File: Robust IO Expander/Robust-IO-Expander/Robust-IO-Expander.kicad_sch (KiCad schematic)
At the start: 69 parts, among them J1 Input Headers, J10 Right SPI In, J11 SPI Terminal, J12 Power Input, J2 CS Inputs, J3 CS Terminal, J4 SPI Inputs, J5 Input Terminal, J6 Output Terminal, J7 Ouput Headers, J8 Power Input, J9 Left SPI Out, U1 MCP23S17_SS, U10 LTV-847S, U11 R-78B3.3-2.0, U12 NUP4202, U13 NUP4202, U14 BZX84C5V1TS-7-F, U15 BZX84C5V1TS-7-F, U2 MCP23S17_SS, U3 LTV-847S, U4 LTV-847S, U5 LTV-847S, U6 LTV-847S, U7 LTV-847S, U8 LTV-847S, U9 LTV-847S

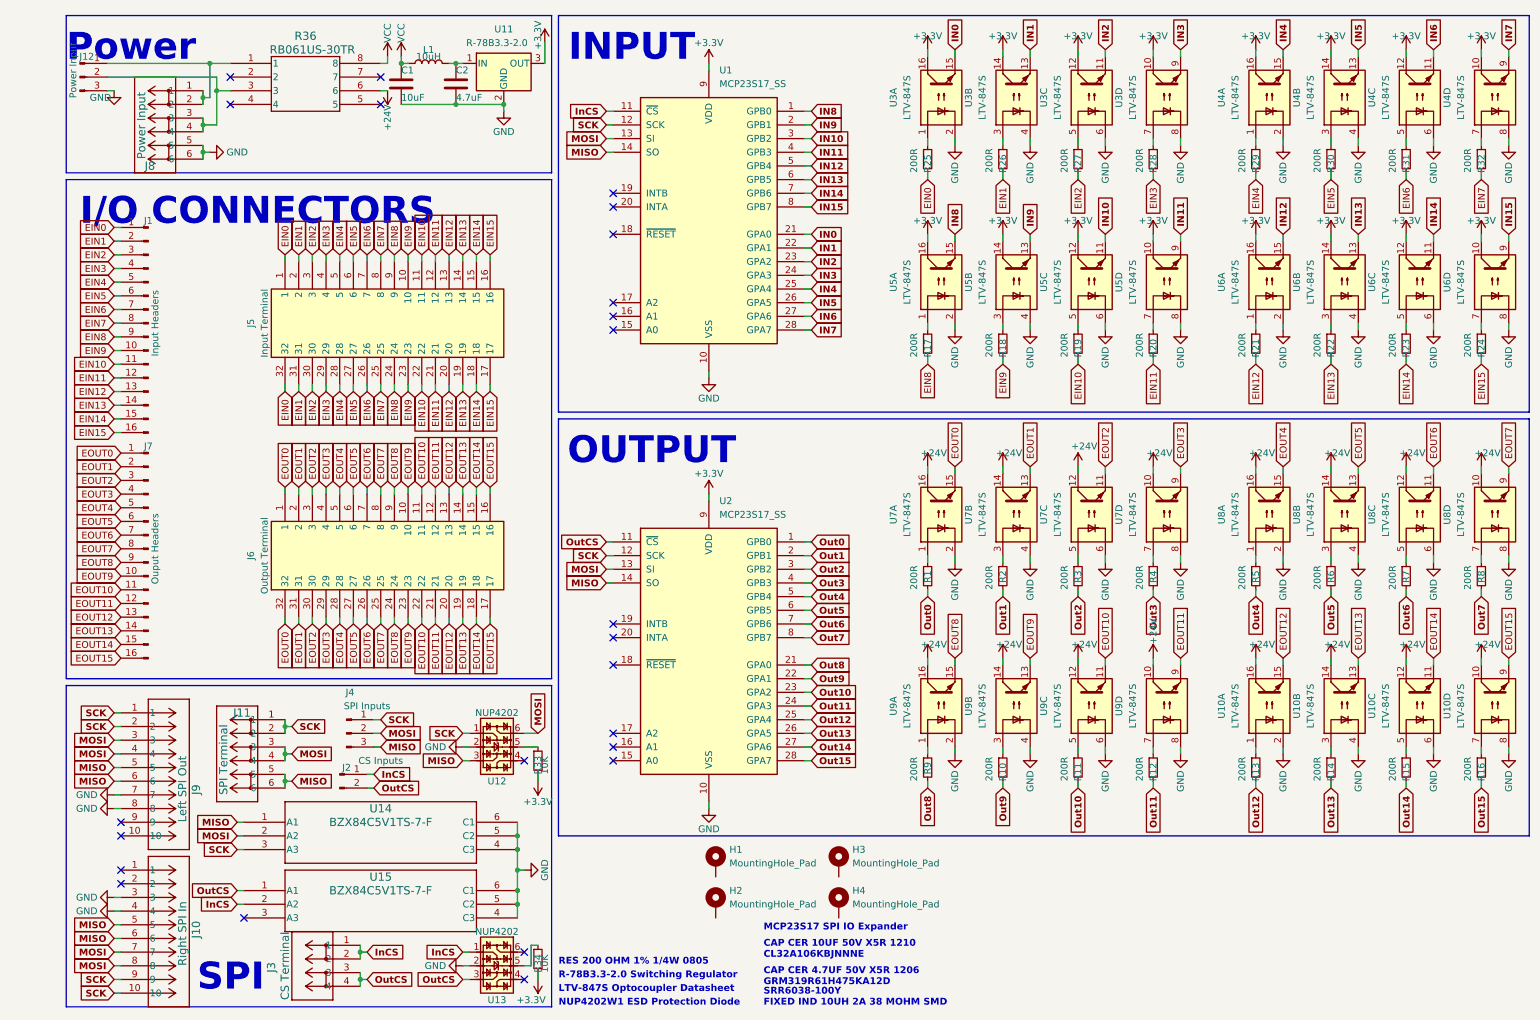
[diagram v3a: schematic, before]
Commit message: Updates
AD 12/11/23
1K Resistors inserted for 200R
0603 components Error correct to 0805
Post DFM Analysis Changes
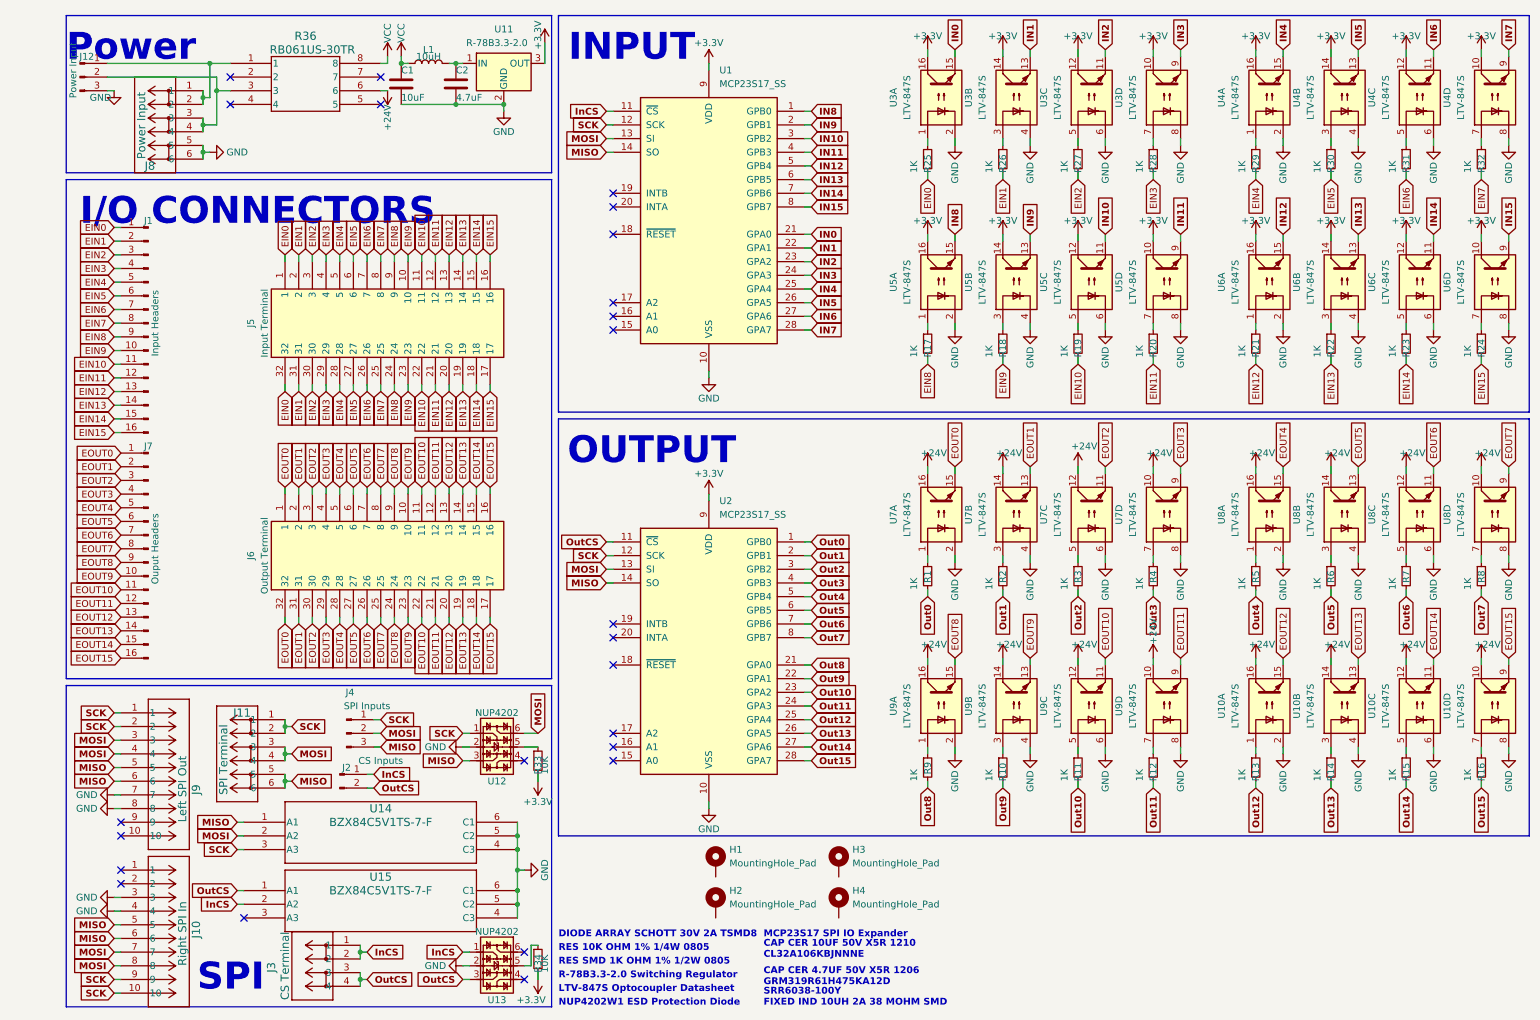
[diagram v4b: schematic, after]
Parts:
- R1, R10, R11, R12, R13, R14, R15, R16, R17, R18, R19, R2, R20, R21, R22, R23, R24, R25, R26, R27, R28, R29, R3, R30, R31, R32, R4, R5, R6, R7, R8, R9: value 200R -> 1K; footprint Resistor_SMD:R_0603_1608Metric_Pad0.98x0.95mm_HandSolder -> Resistor_SMD:R_0805_2012Metric_Pad1.20x1.40mm_HandSolder
- R33, R34: footprint Resistor_SMD:R_0603_1608Metric_Pad0.98x0.95mm_HandSolder -> Resistor_SMD:R_0805_2012Metric_Pad1.20x1.40mm_HandSolder
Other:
- note added: "DIODE ARRAY SCHOTT 30V 2A TSMD8"
- note added: "RES 10K OHM 1% 1/4W 0805"
- note added: "RES SMD 1K OHM 1% 1/2W 0805"
- note removed: "RES 200 OHM 1% 1/4W 0805"
